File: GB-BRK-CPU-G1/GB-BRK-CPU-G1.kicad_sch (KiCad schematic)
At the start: 19 parts

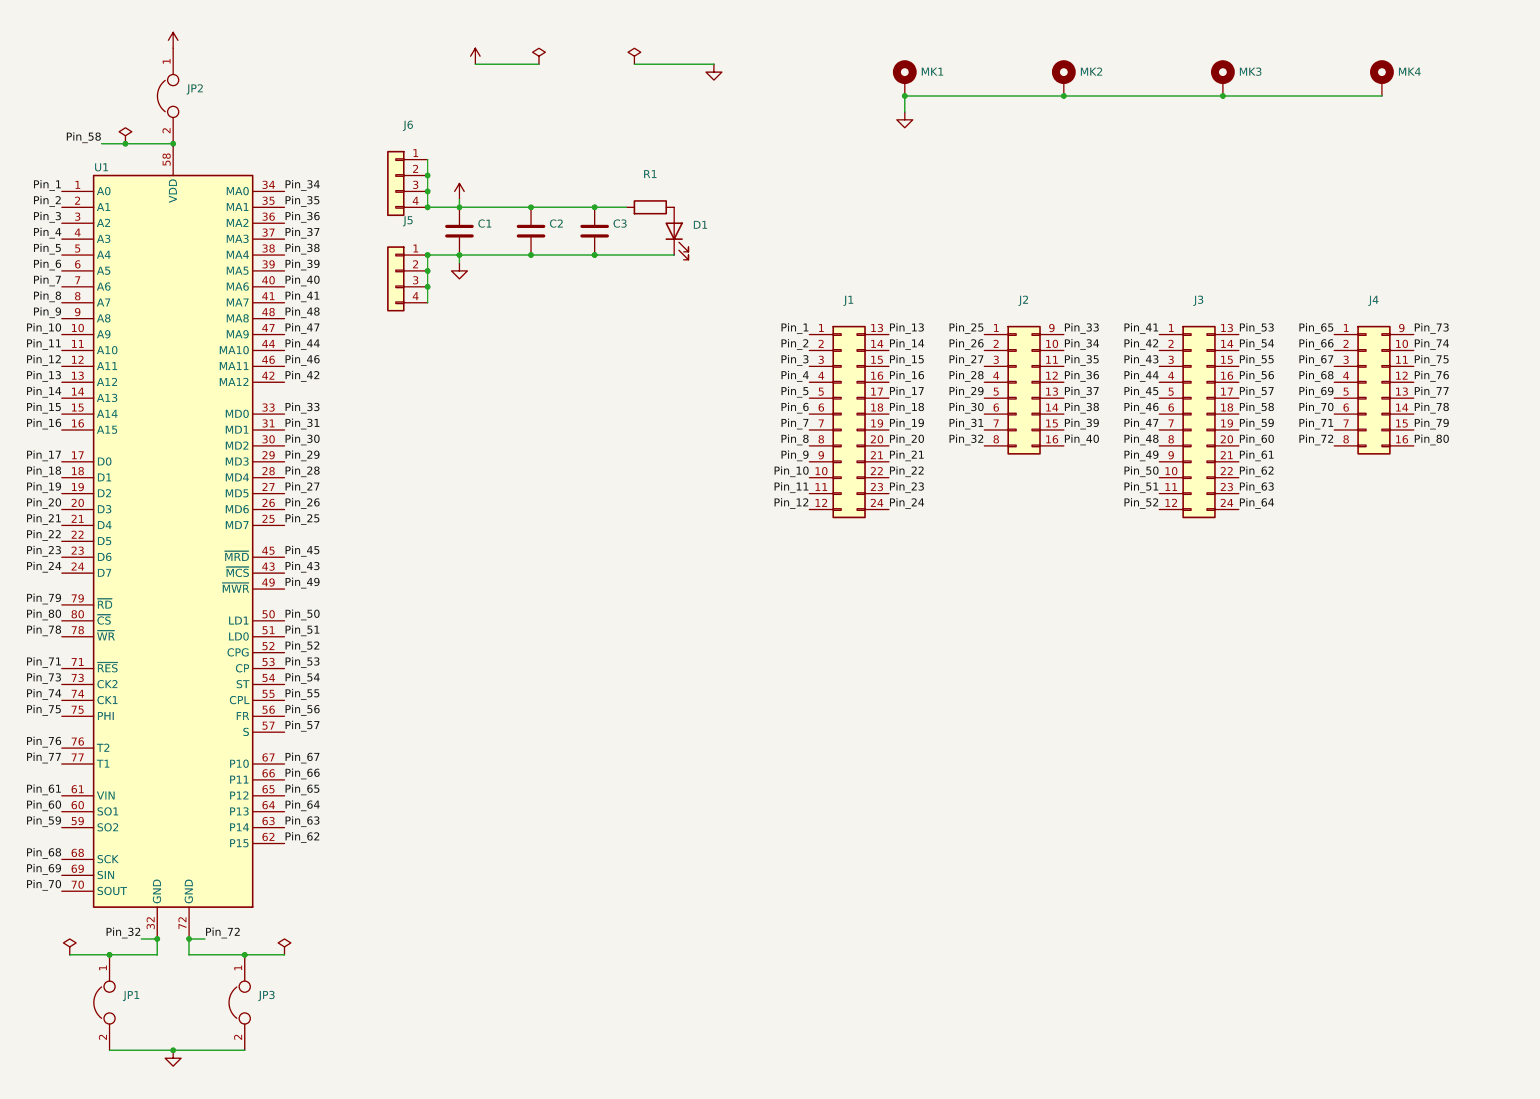
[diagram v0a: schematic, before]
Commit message: Upgrade projects to KiCad 7
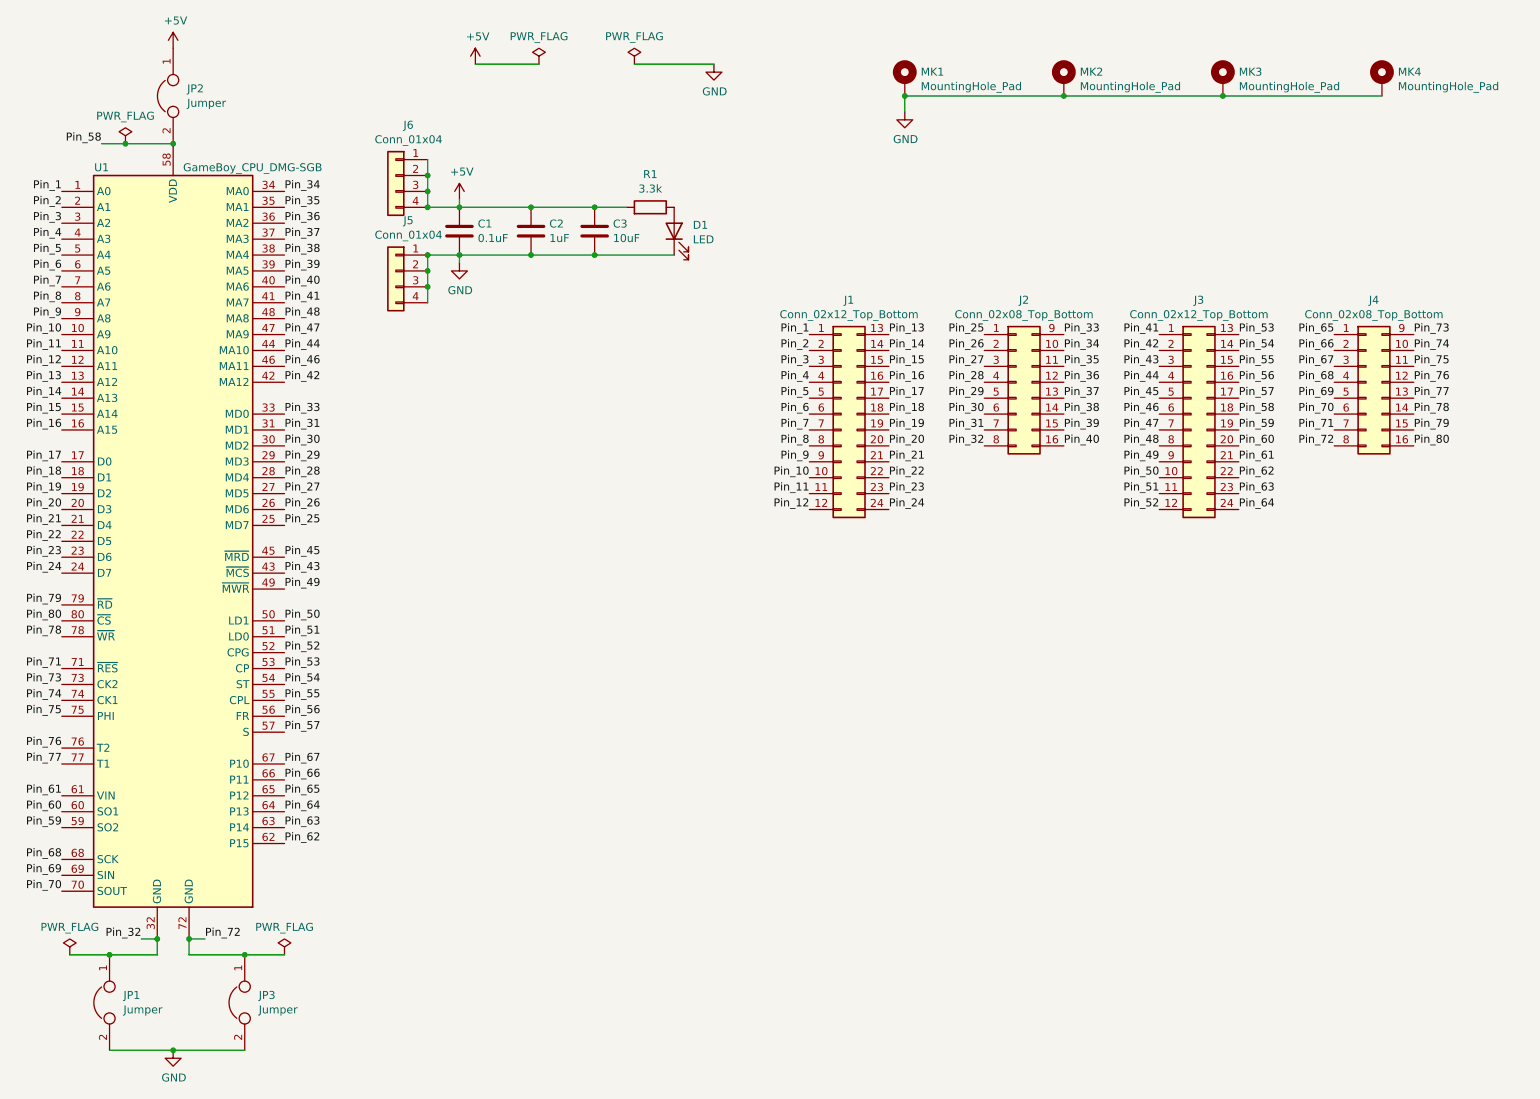
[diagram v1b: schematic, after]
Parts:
- C1: value (none) -> 0.1uF; footprint (none) -> Capacitor_SMD:C_0603_1608Metric
- C2: value (none) -> 1uF; footprint (none) -> Capacitor_SMD:C_0805_2012Metric
- C3: value (none) -> 10uF; footprint (none) -> Capacitor_SMD:C_1206_3216Metric
- D1: value (none) -> LED; footprint (none) -> LED_SMD:LED_0603_1608Metric
- J1, J3: value (none) -> Conn_02x12_Top_Bottom; footprint (none) -> Connector_PinHeader_2.54mm:PinHeader_2x12_P2.54mm_Vertical
- J2, J4: value (none) -> Conn_02x08_Top_Bottom; footprint (none) -> Connector_PinHeader_2.54mm:PinHeader_2x08_P2.54mm_Vertical
- J5, J6: value (none) -> Conn_01x04; footprint (none) -> Connector_PinHeader_2.54mm:PinHeader_1x04_P2.54mm_Vertical
- JP1, JP2, JP3: value (none) -> Jumper; footprint (none) -> Jumper:SolderJumper-2_P1.3mm_Open_TrianglePad1.0x1.5mm
- MK1, MK2, MK3, MK4: value (none) -> MountingHole_Pad; footprint (none) -> MountingHole:MountingHole_3.2mm_M3_Pad_Via
- R1: value (none) -> 3.3k; footprint (none) -> Resistor_SMD:R_0603_1608Metric
- U1: value (none) -> GameBoy_CPU_DMG-SGB; footprint (none) -> Gekkio_Package_QFP:Sharp_QFP-80_14x20mm_P0.8mm
